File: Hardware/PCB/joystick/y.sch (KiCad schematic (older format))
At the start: 25 parts, among them J11 3_pin_Molex_connector, J12 2_pin_Molex_connector, J13 3_pin_Molex_header, J14 2_pin_Molex_header, J6 AudioJack2, J7 AudioJack2, U2 TL074

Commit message: Add gain trimmers and test points
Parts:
- removed R20: 20k, ao_tht:R_Axial_DIN0207_L6.3mm_D2.5mm_P10.16mm_Horizontal, symbol Device:R
- removed unit 1 of U2
- added R20: 10k, ao_tht:R_Axial_DIN0207_L6.3mm_D2.5mm_P10.16mm_Horizontal, symbol ao_symbols:R
- added RV4: 20k, ao_tht:Potentiometer_Bourns_3296W_Vertical_screw_centered, symbol ao_symbols:R_POT_TRIM_3296W
- added TP2: Y_gain, TestPoint:TestPoint_Pad_D2.0mm, symbol Connector:TestPoint
- added unit 1 of U2
- C5: symbol Device:C -> ao_symbols:C; Vendor (none) -> Tayda
- C6: symbol Device:C -> ao_symbols:C
- J11: renamed from J6; Vendor (none) -> Tayda
- J13: renamed from J7; Vendor (none) -> Tayda
- R15, R16, R17, R18, R19, R21, R22, R23, R24, R25, R26, R27, R28: symbol Device:R -> ao_symbols:R; Vendor (none) -> Tayda
- RV5: renamed from RV3; symbol Device:R_POT -> ao_symbols:R_POT; Vendor (none) -> Tayda
- RV6: renamed from RV4; symbol Device:R_POT -> ao_symbols:R_POT; Vendor (none) -> Tayda
- U2: symbol Amplifier_Operational:TL074 -> ao_symbols:TL074; SKU (none) -> A-1138; Vendor (none) -> Tayda
- renumbered J12 to J10, J13 to J12, J11 to J9
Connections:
- net GND: now also U2.3 (+)
- net YRANGEPOT_CCW: now also U2.2 (-)
- net YRANGEPOT_WIPER: now also R20.2
- net at R21.2: now also RV4.1, TP2.1, U2.1
- new net: R20.1, RV4.2, RV4.3

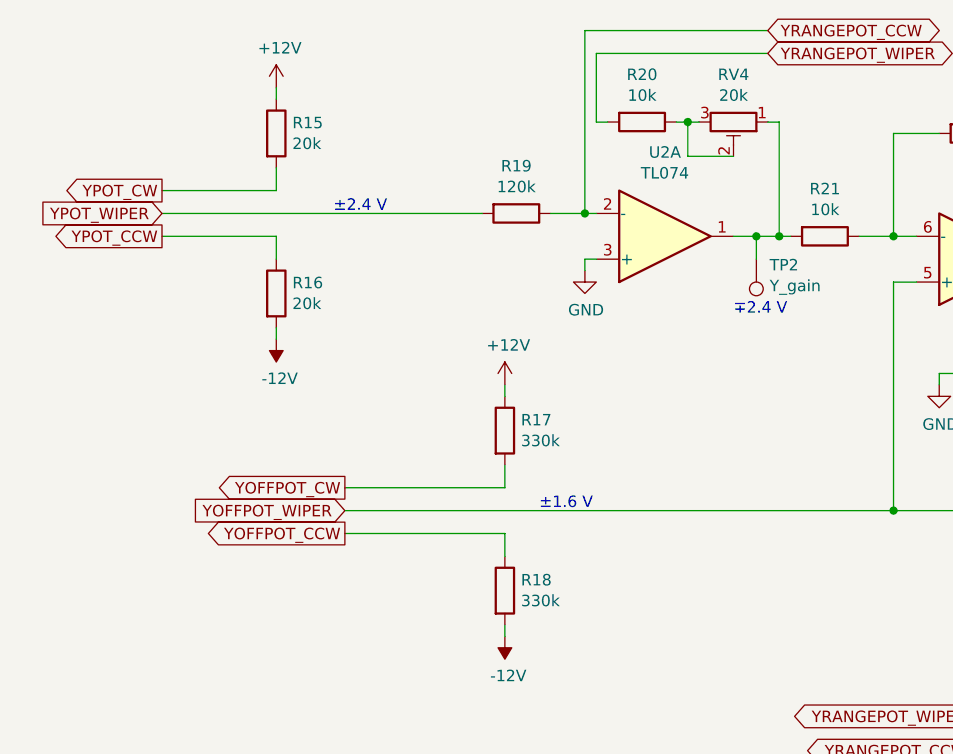
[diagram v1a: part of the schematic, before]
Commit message: Move trimmers to inputs
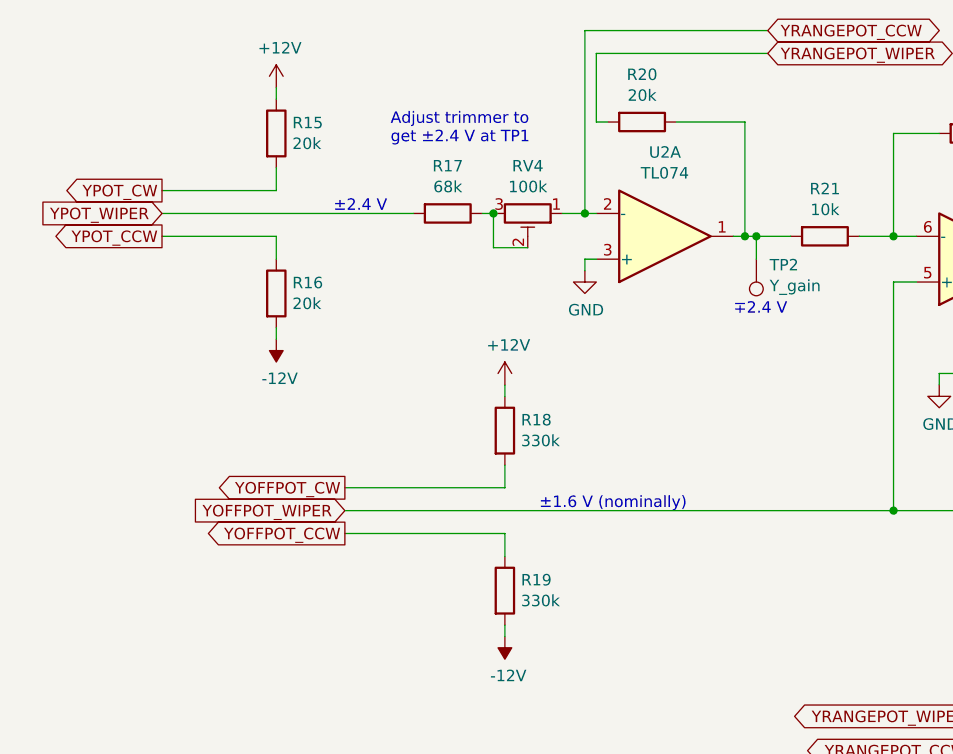
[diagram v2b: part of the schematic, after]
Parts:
- R17: renamed from R19; value 120k -> 68k
- R20: value 10k -> 20k
- RV4: value 20k -> 100k
- renumbered R17 to R18, R18 to R19
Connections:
- net YRANGEPOT_CCW: now also RV4.1; no longer R17.1
- net at R21.2, TP2.1, U2.1: now also R20.1; no longer RV4.1
- net at RV4.2, RV4.3: now also R17.1; no longer R20.1
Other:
- note added: "Adjust trimmer to \nget ±2.4 V at TP1"
- note added: "±1.6 V (nominally)"
- note removed: "±1.6 V"
- moved on the sheet: R17, RV4
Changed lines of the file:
@@
 $EndDescr
-$Comp
-L ao_symbols:R R19
-U 1 1 6158F95D
-P 3400 2150
-F 0 "R19" V 3193 2150 50  0000 C CNN
-F 1 "120k" V 3284 2150 50  0000 C CNN
-F 2 "ao_tht:R_Axial_DIN0207_L6.3mm_D2.5mm_P10.16mm_Horizontal" V 3330 2150 50  0001 C CNN
-F 3 "~" H 3400 2150 50  0001 C CNN
-F 4 "Tayda" H 3400 2150 50  0001 C CNN "Vendor"
-	1    3400 2150
-	0    1    1    0
-$EndComp
 $Comp
 L power:+12V #PWR021
@@
 Wire Wire Line
 	1850 2250 2350 2250
-Wire Wire Line
-	1850 2150 3250 2150
 Wire Wire Line
 	5050 2450 5050 3450
@@
 Text Notes 8400 3100 0    50   ~ 0
 ∓4.8 V + 3(±1.6 V)
-Text Notes 3500 3450 0    50   ~ 0
-±1.6 V
 Text Notes 5900 2350 0    50   ~ 0
 ±4.8 V + 3(±1.6 V)
@@
 	3350 3950 3350 4000
 $Comp
-L ao_symbols:R R17
+L ao_symbols:R R18
 U 1 1 6158FA45
 P 3350 3100
-F 0 "R17" H 3420 3146 50  0000 L CNN
+F 0 "R18" H 3420 3146 50  0000 L CNN
 F 1 "330k" H 3420 3055 50  0000 L CNN
 F 2 "ao_tht:R_Axial_DIN0207_L6.3mm_D2.5mm_P10.16mm_Horizontal" V 3280 3100 50  0001 C CNN
@@
 $EndComp
 $Comp
-L ao_symbols:R R18
+L ao_symbols:R R19
 U 1 1 6158FA4B
 P 3350 3800
-F 0 "R18" H 3420 3846 50  0000 L CNN
+F 0 "R19" H 3420 3846 50  0000 L CNN
 F 1 "330k" H 3420 3755 50  0000 L CNN
 F 2 "ao_tht:R_Axial_DIN0207_L6.3mm_D2.5mm_P10.16mm_Horizontal" V 3280 3800 50  0001 C CNN
@@
 	0    -1   -1   0
 $EndComp
-Wire Wire Line
-	4450 2250 4350 2250
 Connection ~ 4450 2250
 Wire Wire Line
@@
 	-1   0    0    1
 $EndComp
-Wire Wire Line
-	4150 1750 4200 1750
-Connection ~ 4150 1750
-Wire Wire Line
-	4150 1900 4350 1900
-Wire Wire Line
-	4150 1750 4150 1900
 Text Notes 4350 2600 0    50   ~ 0
 ∓2.4 V
@@
 	1    0    0    -1
 $EndComp
-Wire Wire Line
-	3700 1350 3700 2150
-Wire Wire Line
-	3750 1450 3750 1750
-Wire Wire Line
-	4100 1750 4150 1750
-$Comp
-L ao_symbols:R R?
-U 1 1 61846A43
-P 3950 1750
-AR Path="/61846A43" Ref="R?"  Part="1"
-AR Path="/6157E61D/61846A43" Ref="R20"  Part="1"
-F 0 "R20" V 3743 1750 50  0000 C CNN
-F 1 "10k" V 3834 1750 50  0000 C CNN
-F 2 "ao_tht:R_Axial_DIN0207_L6.3mm_D2.5mm_P10.16mm_Horizontal" V 3880 1750 50  0001 C CNN
-F 3 "~" H 3950 1750 50  0001 C CNN
-F 4 "Tayda" H 3950 1750 50  0001 C CNN "Vendor"
-	1    3950 1750
-	0    1    1    0
-$EndComp
-Wire Wire Line
-	4500 1350 3700 1350
-Wire Wire Line
-	4500 1450 3750 1450
-Wire Wire Line
-	3700 2150 3750 2150
-Connection ~ 3700 2150
-Wire Wire Line
-	3800 1750 3750 1750
-Wire Wire Line
-	3550 2150 3700 2150
 $Comp
 L ao_symbols:TL074 U2
@@
 	1    0    0    1
 $EndComp
+Text Notes 3500 3450 0    50   ~ 0
+±1.6 V (nominally)
+Wire Wire Line
+	4450 2250 4400 2250
+Wire Wire Line
+	3300 2300 3450 2300
+Wire Wire Line
+	3300 2150 3300 2300
+Wire Wire Line
+	3600 2150 3700 2150
+Wire Wire Line
+	4100 1750 4400 1750
+Wire Wire Line
+	4400 2250 4350 2250
+Text Notes 2850 1850 0    50   ~ 0
+Adjust trimmer to \nget ±2.4 V at TP1
+Wire Wire Line
+	1850 2150 2950 2150
+Connection ~ 4400 2250
+Wire Wire Line
+	3700 1350 3700 2150
+Wire Wire Line
+	3750 1450 3750 1750
+Wire Wire Line
+	4500 1350 3700 1350
+Wire Wire Line
+	4500 1450 3750 1450
+Wire Wire Line
+	3700 2150 3750 2150
+Connection ~ 3700 2150
+Wire Wire Line
+	3800 1750 3750 1750
+Wire Wire Line
+	4400 1750 4400 2250
+Wire Wire Line
+	3250 2150 3300 2150
 $Comp
 L ao_symbols:R_POT_TRIM_3296W RV?
 U 1 1 61846A57
-P 4350 1750
+P 3450 2150
 AR Path="/61846A57" Ref="RV?"  Part="1"
 AR Path="/6157E61D/61846A57" Ref="RV4"  Part="1"
-F 0 "RV4" V 4143 1750 50  0000 C CNN
-F 1 "20k" V 4234 1750 50  0000 C CNN
-F 2 "ao_tht:Potentiometer_Bourns_3296W_Vertical_screw_centered" H 4350 1750 50  0001 C CNN
-F 3 "~" H 4350 1750 50  0001 C CNN
-F 4 "Tayda" H 4350 1750 50  0001 C CNN "Vendor"
-F 5 "~" H 4350 1750 50  0001 C CNN "SKU"
-	1    4350 1750
-	0    1    1    0
-$EndComp
-Wire Wire Line
-	4450 2250 4550 2250
-Wire Wire Line
-	4500 1750 4550 1750
-Wire Wire Line
-	4550 1750 4550 2250
-Connection ~ 4550 2250
-Wire Wire Line
-	4550 2250 4600 2250
+F 0 "RV4" V 3243 2150 50  0000 C CNN
+F 1 "100k" V 3334 2150 50  0000 C CNN
+F 2 "ao_tht:Potentiometer_Bourns_3296W_Vertical_screw_centered" H 3450 2150 50  0001 C CNN
+F 3 "~" H 3450 2150 50  0001 C CNN
+F 4 "Tayda" H 3450 2150 50  0001 C CNN "Vendor"
+F 5 "~" H 3450 2150 50  0001 C CNN "SKU"
+	1    3450 2150
+	0    1    1    0
+$EndComp
+$Comp
+L ao_symbols:R R?
+U 1 1 61846A43
+P 3950 1750
+AR Path="/61846A43" Ref="R?"  Part="1"
+AR Path="/6157E61D/61846A43" Ref="R20"  Part="1"
+F 0 "R20" V 3743 1750 50  0000 C CNN
+F 1 "20k" V 3834 1750 50  0000 C CNN
+F 2 "ao_tht:R_Axial_DIN0207_L6.3mm_D2.5mm_P10.16mm_Horizontal" V 3880 1750 50  0001 C CNN
+F 3 "~" H 3950 1750 50  0001 C CNN
+F 4 "Tayda" H 3950 1750 50  0001 C CNN "Vendor"
+	1    3950 1750
+	0    1    1    0
+$EndComp
+$Comp
+L ao_symbols:R R17
+U 1 1 6158F95D
+P 3100 2150
+F 0 "R17" V 2893 2150 50  0000 C CNN
+F 1 "68k" V 2984 2150 50  0000 C CNN
+F 2 "ao_tht:R_Axial_DIN0207_L6.3mm_D2.5mm_P10.16mm_Horizontal" V 3030 2150 50  0001 C CNN
+F 3 "~" H 3100 2150 50  0001 C CNN
+F 4 "Tayda" H 3100 2150 50  0001 C CNN "Vendor"
+	1    3100 2150
+	0    1    1    0
+$EndComp
+Connection ~ 3300 2150
+Wire Wire Line
+	4450 2250 4600 2250
 $EndSCHEMATC

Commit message: More tweaks, build.md
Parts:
- R18, R19: value 330k -> 300k
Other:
- note added: "±1.6 V (approx.,\ndepending on actual\npot value, PSU voltage,\nand Schottky diode\ndrop)"
- note removed: "±1.6 V (nominally)"
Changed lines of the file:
@@
 P 3350 3100
 F 0 "R18" H 3420 3146 50  0000 L CNN
-F 1 "330k" H 3420 3055 50  0000 L CNN
+F 1 "300k" H 3420 3055 50  0000 L CNN
 F 2 "ao_tht:R_Axial_DIN0207_L6.3mm_D2.5mm_P10.16mm_Horizontal" V 3280 3100 50  0001 C CNN
 F 3 "~" H 3350 3100 50  0001 C CNN
@@
 P 3350 3800
 F 0 "R19" H 3420 3846 50  0000 L CNN
-F 1 "330k" H 3420 3755 50  0000 L CNN
+F 1 "300k" H 3420 3755 50  0000 L CNN
 F 2 "ao_tht:R_Axial_DIN0207_L6.3mm_D2.5mm_P10.16mm_Horizontal" V 3280 3800 50  0001 C CNN
 F 3 "~" H 3350 3800 50  0001 C CNN
@@
 	1    0    0    1
 $EndComp
-Text Notes 3500 3450 0    50   ~ 0
-±1.6 V (nominally)
+Text Notes 3850 3900 0    50   ~ 0
+±1.6 V (approx.,\ndepending on actual\npot value, PSU voltage,\nand Schottky diode\ndrop)
 Wire Wire Line
 	4450 2250 4400 2250

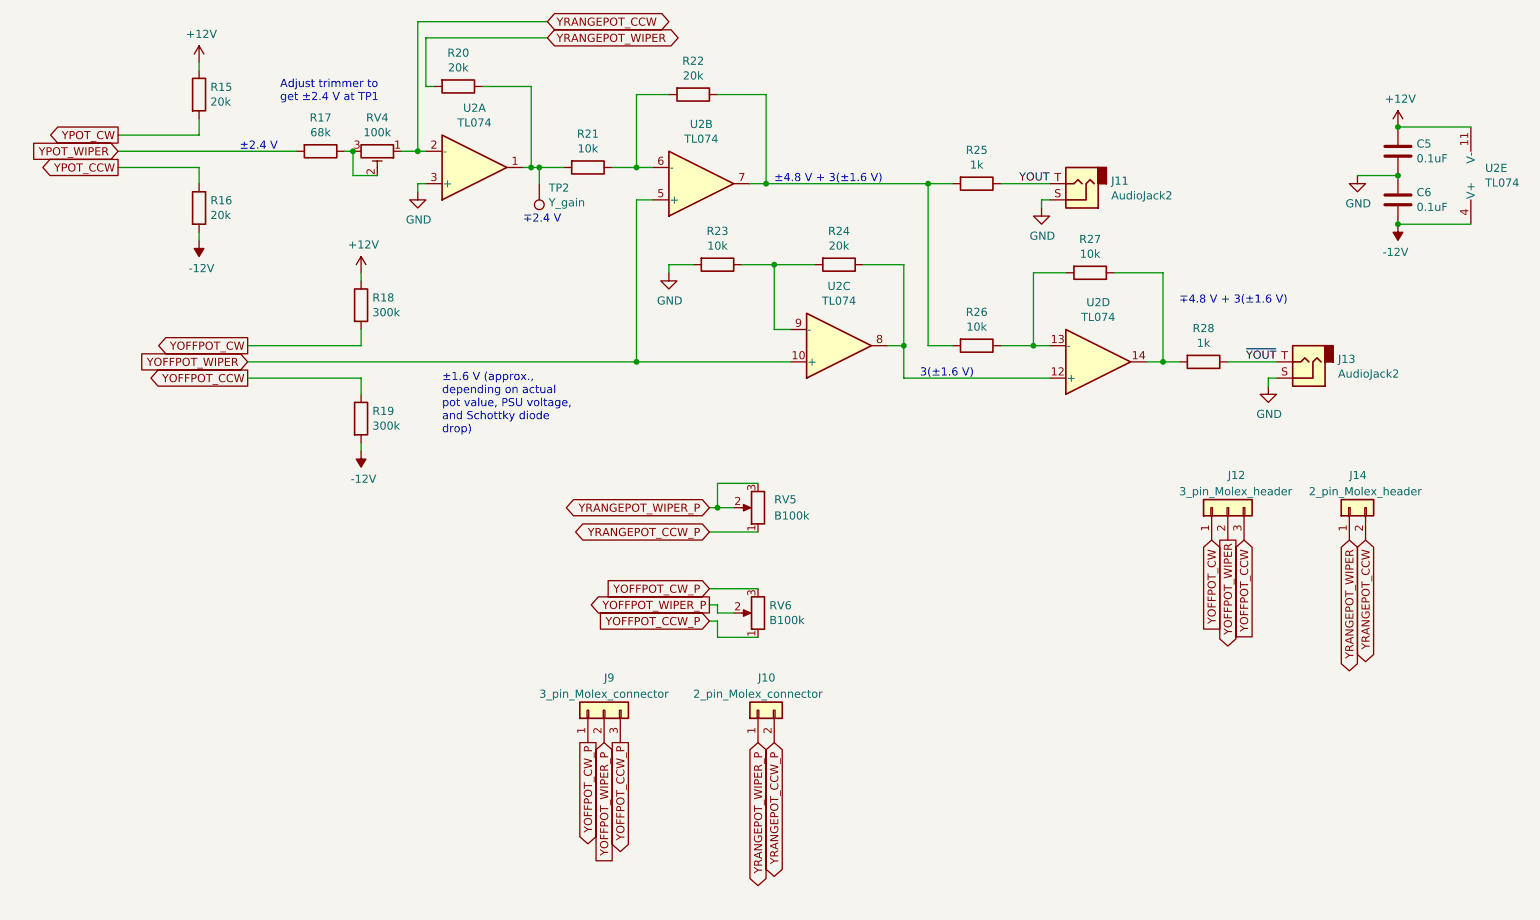
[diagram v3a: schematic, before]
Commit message: Change voltage ranges
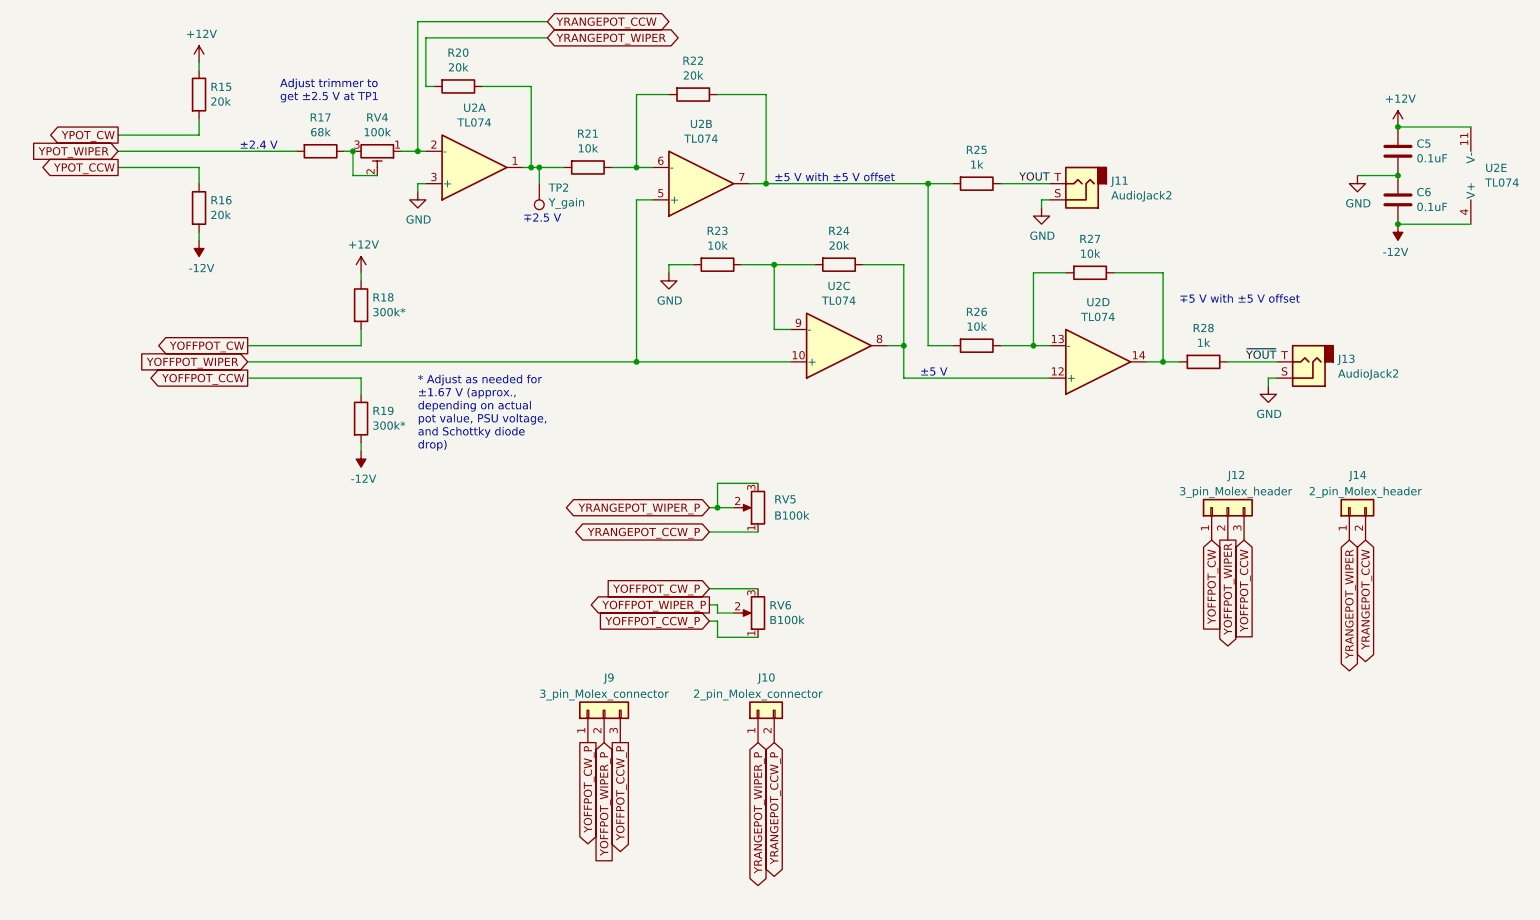
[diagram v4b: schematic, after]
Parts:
- R18, R19: value 300k -> 300k*
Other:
- note added: "* Adjust as needed for\n±1.67 V (approx.,\ndepending on actual\npot value, PSU voltage,\nand Schottky diode\ndrop)"
- note added: "Adjust trimmer to \nget ±2.5 V at TP1"
- note added: "±5 V"
- note added: "±5 V with ±5 V offset"
- note added: "∓2.5 V"
- note added: "∓5 V with ±5 V offset"
- note removed: "3(±1.6 V)"
- note removed: "Adjust trimmer to \nget ±2.4 V at TP1"
- note removed: "±1.6 V (approx.,\ndepending on actual\npot value, PSU voltage,\nand Schottky diode\ndrop)"
- note removed: "±4.8 V + 3(±1.6 V)"
- note removed: "∓2.4 V"
- note removed: "∓4.8 V + 3(±1.6 V)"
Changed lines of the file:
@@
 $EndComp
 Text Notes 8400 3100 0    50   ~ 0
-∓4.8 V + 3(±1.6 V)
+∓5 V with ±5 V offset
 Text Notes 5900 2350 0    50   ~ 0
-±4.8 V + 3(±1.6 V)
+±5 V with ±5 V offset
 Text Notes 6800 3550 0    50   ~ 0
-3(±1.6 V)
+±5 V
 Wire Wire Line
 	2650 3450 5050 3450
@@
 P 3350 3100
 F 0 "R18" H 3420 3146 50  0000 L CNN
-F 1 "300k" H 3420 3055 50  0000 L CNN
+F 1 "300k*" H 3420 3055 50  0000 L CNN
 F 2 "ao_tht:R_Axial_DIN0207_L6.3mm_D2.5mm_P10.16mm_Horizontal" V 3280 3100 50  0001 C CNN
 F 3 "~" H 3350 3100 50  0001 C CNN
@@
 P 3350 3800
 F 0 "R19" H 3420 3846 50  0000 L CNN
-F 1 "300k" H 3420 3755 50  0000 L CNN
+F 1 "300k*" H 3420 3755 50  0000 L CNN
 F 2 "ao_tht:R_Axial_DIN0207_L6.3mm_D2.5mm_P10.16mm_Horizontal" V 3280 3800 50  0001 C CNN
 F 3 "~" H 3350 3800 50  0001 C CNN
@@
 $EndComp
 Text Notes 4350 2600 0    50   ~ 0
-∓2.4 V
+∓2.5 V
 Wire Wire Line
 	3700 2350 3700 2400
@@
 	1    0    0    1
 $EndComp
-Text Notes 3850 3900 0    50   ~ 0
-±1.6 V (approx.,\ndepending on actual\npot value, PSU voltage,\nand Schottky diode\ndrop)
+Text Notes 3700 4000 0    50   ~ 0
+* Adjust as needed for\n±1.67 V (approx.,\ndepending on actual\npot value, PSU voltage,\nand Schottky diode\ndrop)
 Wire Wire Line
 	4450 2250 4400 2250
@@
 	4400 2250 4350 2250
 Text Notes 2850 1850 0    50   ~ 0
-Adjust trimmer to \nget ±2.4 V at TP1
+Adjust trimmer to \nget ±2.5 V at TP1
 Wire Wire Line
 	1850 2150 2950 2150

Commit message: Move trimmers and TPs to back
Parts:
- RV4: footprint ao_tht:Potentiometer_Bourns_3296W_Vertical_screw_centered -> ao_tht:Potentiometer_Bourns_3296W_Vertical_standard
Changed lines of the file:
@@
 F 0 "RV4" V 3243 2150 50  0000 C CNN
 F 1 "100k" V 3334 2150 50  0000 C CNN
-F 2 "ao_tht:Potentiometer_Bourns_3296W_Vertical_screw_centered" H 3450 2150 50  0001 C CNN
+F 2 "ao_tht:Potentiometer_Bourns_3296W_Vertical_standard" H 3450 2150 50  0001 C CNN
 F 3 "~" H 3450 2150 50  0001 C CNN
 F 4 "Tayda" H 3450 2150 50  0001 C CNN "Vendor"

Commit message: Update docs, generate Gerbers
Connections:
- net +12V: now also C6.2, U2.4 (V+); no longer C5.1, U2.11 (V-)
- net -12V: now also C5.1, U2.11 (V-); no longer C6.2, U2.4 (V+)
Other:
- moved on the sheet: C5, C6
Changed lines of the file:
@@
 L ao_symbols:C C?
 U 1 1 615950D6
-P 9750 2150
+P 9750 2450
 AR Path="/615950D6" Ref="C?"  Part="1"
 AR Path="/6157E61D/615950D6" Ref="C5"  Part="1"
-F 0 "C5" H 9865 2196 50  0000 L CNN
-F 1 "0.1uF" H 9865 2105 50  0000 L CNN
+F 0 "C5" H 9550 2500 50  0000 L CNN
+F 1 "0.1uF" H 9450 2400 50  0000 L CNN
+F 2 "ao_tht:C_Disc_D3.0mm_W1.6mm_P2.50mm" H 9788 2300 50  0001 C CNN
+F 3 "~" H 9750 2450 50  0001 C CNN
+F 4 "Tayda" H 9750 2450 50  0001 C CNN "Vendor"
+	1    9750 2450
+	-1   0    0    1
+$EndComp
+$Comp
+L ao_symbols:C C?
+U 1 1 615950DC
+P 9750 2150
+AR Path="/615950DC" Ref="C?"  Part="1"
+AR Path="/6157E61D/615950DC" Ref="C6"  Part="1"
+F 0 "C6" H 9550 2200 50  0000 L CNN
+F 1 "0.1uF" H 9450 2100 50  0000 L CNN
 F 2 "ao_tht:C_Disc_D3.0mm_W1.6mm_P2.50mm" H 9788 2000 50  0001 C CNN
 F 3 "~" H 9750 2150 50  0001 C CNN
-F 4 "Tayda" H 9750 2150 50  0001 C CNN "Vendor"
 	1    9750 2150
-	1    0    0    -1
-$EndComp
-$Comp
-L ao_symbols:C C?
-U 1 1 615950DC
-P 9750 2450
-AR Path="/615950DC" Ref="C?"  Part="1"
-AR Path="/6157E61D/615950DC" Ref="C6"  Part="1"
-F 0 "C6" H 9865 2496 50  0000 L CNN
-F 1 "0.1uF" H 9865 2405 50  0000 L CNN
-F 2 "ao_tht:C_Disc_D3.0mm_W1.6mm_P2.50mm" H 9788 2300 50  0001 C CNN
-F 3 "~" H 9750 2450 50  0001 C CNN
-	1    9750 2450
-	1    0    0    -1
+	-1   0    0    1
 $EndComp
 $Comp
@@
 Wire Wire Line
 	9500 2300 9750 2300
-Connection ~ 9750 2300
 $Comp
 L power:+12V #PWR?
@@
 F 5 "Tayda" H 10100 2300 50  0001 C CNN "Vendor"
 	5    10100 2300
-	-1   0    0    1
+	-1   0    0    -1
 $EndComp
 Wire Wire Line
 	10200 2000 9750 2000
-Connection ~ 9750 2000
 Wire Wire Line
 	10200 2600 9750 2600
@@
 Wire Wire Line
 	4450 2250 4600 2250
+Connection ~ 9750 2300
+Connection ~ 9750 2000
 $EndSCHEMATC

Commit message: copy and paste typo
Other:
- note added: "Adjust trimmer to \nget ±2.5 V at TP2"
- note removed: "Adjust trimmer to \nget ±2.5 V at TP1"
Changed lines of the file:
@@
 	4400 2250 4350 2250
 Text Notes 2850 1850 0    50   ~ 0
-Adjust trimmer to \nget ±2.5 V at TP1
+Adjust trimmer to \nget ±2.5 V at TP2
 Wire Wire Line
 	1850 2150 2950 2150
